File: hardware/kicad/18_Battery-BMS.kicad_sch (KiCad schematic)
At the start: 29 parts, among them U80 BQ7694202PFBR

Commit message: starting erc check
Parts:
- C110, C111, C112, C113, C114, C119, C121: footprint Capacitor_SMD:C_0603_1608Metric -> 5v rail sm-easyedapro:C0603
- C115: footprint Capacitor_SMD:C_0603_1608Metric -> 5v rail sm-easyedapro:C0402; LCSC Part Name (none) -> 100pF ±5% 50V; Manufacturer (none) -> FOJAN(富捷); Manufacturer Part (none) -> FCC0402N101J500AT; Supplier (none) -> LCSC; Supplier Part (none) -> C5137573
- C120: footprint Capacitor_SMD:C_0603_1608Metric -> 5v rail sm-easyedapro:C0603; Manufacturer SAMSUNG(三星) -> HRE(芯声); Manufacturer Part CL10B105KB8NQNC -> CGA0603X5R105K500JT; Supplier Part C5199872 -> C6119852
- D19, D20, D21, D22: footprint Diode_SMD:SOD-123 -> 5v rail sm-easyedapro:SOD-123_L2.8-W1.8-LS3.7-RD
- R172, R173, R174, R175, R185, R187, R191, R192, R193, R194, R195: footprint Resistor_SMD:R_0603_1608Metric -> 5v rail sm-easyedapro:R0603
- R190: footprint Resistor_SMD:R_1206_3216Metric -> 5v rail sm-easyedapro:R1206
- U80: footprint Package_QFP:TQFP-48_7x7mm_P0.5mm -> 5v rail sm-easyedapro:TQFP-48_L7.0-W7.0-P0.50-LS9.0-TL
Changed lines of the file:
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@@
 			)
 		)
-		(property "Footprint" "Diode_SMD:SOD-123"
+		(property "Footprint" "5v rail sm-easyedapro:SOD-123_L2.8-W1.8-LS3.7-RD"
 			(at 218.44 31.75 0)
 			(effects
@@
 			)
 		)
-		(property "Footprint" "Resistor_SMD:R_0603_1608Metric"
+		(property "Footprint" "5v rail sm-easyedapro:R0603"
 			(at 157.48 160.02 0)
 			(effects
@@
 			)
 		)
-		(property "Footprint" "Diode_SMD:SOD-123"
+		(property "Footprint" "5v rail sm-easyedapro:SOD-123_L2.8-W1.8-LS3.7-RD"
 			(at 60.96 128.27 0)
 			(effects
@@
 			)
 		)
-		(property "Footprint" "Resistor_SMD:R_0603_1608Metric"
+		(property "Footprint" "5v rail sm-easyedapro:R0603"
 			(at 62.23 90.17 0)
 			(effects
@@
 			)
 		)
-		(property "Footprint" "Package_QFP:TQFP-48_7x7mm_P0.5mm"
+		(property "Footprint" "5v rail sm-easyedapro:TQFP-48_L7.0-W7.0-P0.50-LS9.0-TL"
 			(at 220.98 95.25 0)
 			(effects
@@
 			)
 		)
-		(property "Footprint" "Resistor_SMD:R_0603_1608Metric"
+		(property "Footprint" "5v rail sm-easyedapro:R0603"
 			(at 184.15 161.29 0)
 			(effects
@@
 			)
 		)
-		(property "Footprint" "Capacitor_SMD:C_0603_1608Metric"
+		(property "Footprint" "5v rail sm-easyedapro:C0603"
 			(at 302.26 54.61 0)
 			(effects
@@
 			)
 		)
-		(property "Footprint" "Capacitor_SMD:C_0603_1608Metric"
+		(property "Footprint" "5v rail sm-easyedapro:C0603"
 			(at 275.59 53.34 0)
 			(effects
@@
 			)
 		)
-		(property "Footprint" "Resistor_SMD:R_0603_1608Metric"
+		(property "Footprint" "5v rail sm-easyedapro:R0603"
 			(at 62.23 55.88 0)
 			(effects
@@
 			)
 		)
-		(property "Footprint" "Capacitor_SMD:C_0603_1608Metric"
+		(property "Footprint" "5v rail sm-easyedapro:C0402"
 			(at 171.45 147.32 0)
 			(effects
@@
 			)
 		)
-		(property "Datasheet" ""
+		(property "Datasheet" "https://item.szlcsc.com/datasheet/FCC0402N101J500AT/5747025.html"
 			(at 171.45 147.32 0)
 			(effects
@@
 			)
 		)
-		(property "Description" ""
+		(property "Description" "Capacitance:100pF Tolerance:±5% Tolerance:±5% Voltage Rating:50V Temperature Coefficient:C0G"
 			(at 171.45 147.32 0)
 			(effects
@@
 			)
 		)
-		(property "Manufacturer Part" ""
+		(property "Manufacturer Part" "FCC0402N101J500AT"
 			(at 171.45 147.32 0)
 			(effects
@@
 			)
 		)
-		(property "Manufacturer" ""
+		(property "Manufacturer" "FOJAN(富捷)"
 			(at 171.45 147.32 0)
 			(effects
@@
 			)
 		)
-		(property "Supplier Part" ""
+		(property "Supplier Part" "C5137573"
 			(at 171.45 147.32 0)
 			(effects
@@
 			)
 		)
-		(property "Supplier" ""
+		(property "Supplier" "LCSC"
 			(at 171.45 147.32 0)
 			(effects
@@
 			)
 		)
-		(property "LCSC Part Name" ""
+		(property "LCSC Part Name" "100pF ±5% 50V"
 			(at 171.45 147.32 0)
 			(effects
@@
 			)
 		)
-		(property "Footprint" "Capacitor_SMD:C_0603_1608Metric"
+		(property "Footprint" "5v rail sm-easyedapro:C0603"
 			(at 99.06 128.27 0)
 			(effects
@@
 			)
 		)
-		(property "Footprint" "Capacitor_SMD:C_0603_1608Metric"
+		(property "Footprint" "5v rail sm-easyedapro:C0603"
 			(at 78.74 81.28 0)
 			(effects
@@
 			)
 		)
-		(property "Footprint" "Resistor_SMD:R_0603_1608Metric"
+		(property "Footprint" "5v rail sm-easyedapro:R0603"
 			(at 288.29 80.01 0)
 			(effects
@@
 			)
 		)
-		(property "Footprint" "Resistor_SMD:R_0603_1608Metric"
+		(property "Footprint" "5v rail sm-easyedapro:R0603"
 			(at 62.23 102.87 0)
 			(effects
@@
 			)
 		)
-		(property "Footprint" "Diode_SMD:SOD-123"
+		(property "Footprint" "5v rail sm-easyedapro:SOD-123_L2.8-W1.8-LS3.7-RD"
 			(at 218.44 44.45 0)
 			(effects
@@
 			)
 		)
-		(property "Footprint" "Resistor_SMD:R_0603_1608Metric"
+		(property "Footprint" "5v rail sm-easyedapro:R0603"
 			(at 275.59 97.79 0)
 			(effects
@@
 			)
 		)
-		(property "Footprint" "Capacitor_SMD:C_0603_1608Metric"
+		(property "Footprint" "5v rail sm-easyedapro:C0603"
 			(at 289.56 54.61 0)
 			(effects
@@
 			)
 		)
-		(property "Datasheet" "https://item.szlcsc.com/datasheet/CL10B105KB8NQNC/5885909.html"
+		(property "Datasheet" "https://item.szlcsc.com/datasheet/CGA0603X5R105K500JT/7062558.html"
 			(at 289.56 54.61 0)
 			(effects
@@
 			)
 		)
-		(property "Description" "Capacitance:1uF Tolerance:±10% Tolerance:±10% Voltage Rating:50V Temperature Coefficient:X7R"
+		(property "Description" "Capacitance:1uF Tolerance:±10% Tolerance:±10% Voltage Rating:50V Temperature Coefficient:X5R"
 			(at 289.56 54.61 90)
 			(effects
@@
 			)
 		)
-		(property "Manufacturer Part" "CL10B105KB8NQNC"
+		(property "Manufacturer Part" "CGA0603X5R105K500JT"
 			(at 289.56 54.61 0)
 			(effects
@@
 			)
 		)
-		(property "Manufacturer" "SAMSUNG(三星)"
+		(property "Manufacturer" "HRE(芯声)"
 			(at 289.56 54.61 0)
 			(effects
@@
 			)
 		)
-		(property "Supplier Part" "C5199872"
+		(property "Supplier Part" "C6119852"
 			(at 289.56 54.61 0)
 			(effects
@@
 			)
 		)
-		(property "Footprint" "Capacitor_SMD:C_0603_1608Metric"
+		(property "Footprint" "5v rail sm-easyedapro:C0603"
 			(at 171.45 135.89 0)
 			(effects
@@
 			)
 		)
-		(property "Footprint" "Diode_SMD:SOD-123"
+		(property "Footprint" "5v rail sm-easyedapro:SOD-123_L2.8-W1.8-LS3.7-RD"
 			(at 78.74 128.27 0)
 			(effects
@@
 			)
 		)
-		(property "Footprint" "Resistor_SMD:R_0603_1608Metric"
+		(property "Footprint" "5v rail sm-easyedapro:R0603"
 			(at 288.29 90.17 0)
 			(effects
@@
 			)
 		)
-		(property "Datasheet" ""
+		(property "Datasheet" "~"
 			(at 203.2 44.45 0)
 			(effects
@@
 			)
 		)
-		(property "Description" ""
+		(property "Description" "Jumper, 2-pole, open"
 			(at 203.2 44.45 0)
 			(effects
@@
 			)
 		)
-		(property "Footprint" "Resistor_SMD:R_0603_1608Metric"
+		(property "Footprint" "5v rail sm-easyedapro:R0603"
 			(at 275.59 106.68 0)
 			(effects
@@
 			)
 		)
-		(property "Footprint" "Resistor_SMD:R_0603_1608Metric"
+		(property "Footprint" "5v rail sm-easyedapro:R0603"
 			(at 62.23 73.66 0)
 			(effects
@@
 			)
 		)
-		(property "Footprint" "Resistor_SMD:R_0603_1608Metric"
+		(property "Footprint" "5v rail sm-easyedapro:R0603"
 			(at 318.77 111.76 0)
 			(effects
@@
 			)
 		)
-		(property "Footprint" "Resistor_SMD:R_1206_3216Metric"
+		(property "Footprint" "5v rail sm-easyedapro:R1206"
 			(at 245.11 44.45 0)
 			(effects
@@
 			)
 		)
-		(property "Footprint" "Capacitor_SMD:C_0603_1608Metric"
+		(property "Footprint" "5v rail sm-easyedapro:C0603"
 			(at 78.74 64.77 0)
 			(effects
@@
 			)
 		)
-		(property "Footprint" "Capacitor_SMD:C_0603_1608Metric"
+		(property "Footprint" "5v rail sm-easyedapro:C0603"
 			(at 111.76 96.52 0)
 			(effects

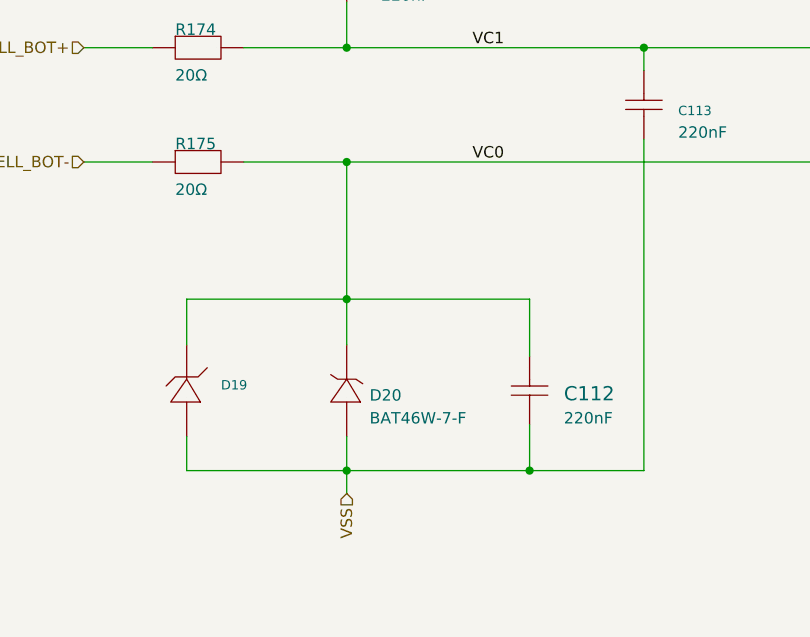
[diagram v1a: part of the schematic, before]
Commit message: usb c diodiding
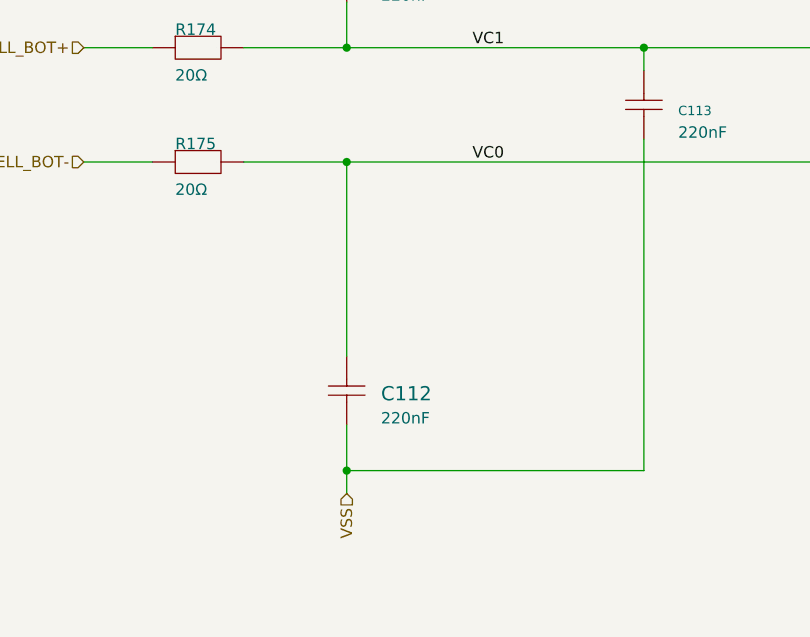
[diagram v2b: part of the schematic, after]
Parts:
- removed D19: MMSZ4685T1G, 5v rail sm-easyedapro:SOD-123_L2.8-W1.8-LS3.7-RD, symbol 5v rail sm-easyedapro:MMSZ4685T1G
- removed D20: BAT46W-7-F, 5v rail sm-easyedapro:SOD-123_L2.8-W1.8-LS3.7-RD, symbol 5v rail sm-easyedapro:BAT46W-7-F
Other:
- moved on the sheet: C112

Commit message: pre switching to native footprints for caps and resistors
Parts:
- removed C110, C111, C112, C113: 220nF, 5v rail sm-easyedapro:C0603, symbol 5v rail sm-easyedapro:CC0603KRX7R9BB224
- removed C121: 100pF, 5v rail sm-easyedapro:C0603, symbol 5v rail sm-easyedapro:CC0603JRNPO9BN101
- removed R172, R173, R174: 20Ω, 5v rail sm-easyedapro:R0603, symbol 5v rail sm-easyedapro:FRC0603F20R0TS
- removed R191: 82kΩ, 5v rail sm-easyedapro:R0603, symbol 5v rail sm-easyedapro:FRC0603F8202TS
- removed R192: 100kΩ, 5v rail sm-easyedapro:R0603, symbol 5v rail sm-easyedapro:FRC0603J104 TS
- removed R193, R194, R195: 10kΩ, 5v rail sm-easyedapro:R0603, symbol 5v rail sm-easyedapro:0603WAF1002T5E
- added C3501, C3502, C3503, C3505: 220nF, Capacitor_SMD:C_0402_1005Metric, symbol Device:C
- added C3504: 100pF, Capacitor_SMD:C_0402_1005Metric, symbol Device:C
- added R3501, R3502, R3503: 20Ω, Resistor_SMD:R_0603_1608Metric, symbol Device:R
- added R3504, R3505, R3508: 10k, Resistor_SMD:R_0402_1005Metric, symbol Device:R
- added R3506: 100k, Resistor_SMD:R_0402_1005Metric, symbol Device:R
- added R3507: 82k, Resistor_SMD:R_0402_1005Metric, symbol Device:R
- renumbered U79 to U?
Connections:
- net ALERT: now also R3508.1
- net ALERT_PULLUP: now also R3508.2
- net BAL-CELL-2: now also R3502.1
- net BAL-CELL-TOP: now also JP4.1 (A), R3501.1; no longer U?.2 (B)
- net BAL_CELL_BOT+: now also R3503.1
- net BQ-BAT: now also U?.2 (B); no longer JP4.1 (A)
- net PACK+: now also R3504.2, R3505.2
- net RST_SHUT: now also R3506.1
- net VC0: now also C3505.2
- net VC1: now also C3501.1, C3502.2, R3503.2
- net VC3: now also C3502.1, C3503.2, R3502.2
- net VC4: now also C3503.1, R3501.2
- net VSS: now also C3501.2, C3504.2, C3505.1, R3506.2, R3507.2
- net at D21.2: now also U?.1 (A); no longer JP4.2 (B)
- net at U80.34 (REG2), U80.35 (REG1): now also R3507.1
- net at U80.41 (LD): now also R3505.1
- net at U80.42 (PACK): now also R3504.1
- net at C119.2, C120.2, R190.1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: now also C3504.1
- net at D22.2: now also JP4.2 (B); no longer U?.1 (A)

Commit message: updating symbols to use kicad footprints where possible
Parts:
- C114, C119, C120: footprint 5v rail sm-easyedapro:C0603 -> Capacitor_SMD:C_0603_1608Metric
- C115: footprint 5v rail sm-easyedapro:C0402 -> Capacitor_SMD:C_0402_1005Metric
- R175, R185, R187: footprint 5v rail sm-easyedapro:R0603 -> Resistor_SMD:R_0603_1608Metric
- R190: footprint 5v rail sm-easyedapro:R1206 -> Resistor_SMD:R_1206_3216Metric
- gave numbers to parts that had none: 1
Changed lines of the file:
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@@
 			)
 		)
-		(property "Footprint" "5v rail sm-easyedapro:R0603"
+		(property "Footprint" "Resistor_SMD:R_0603_1608Metric"
 			(at 157.48 160.02 0)
 			(effects
@@
 			)
 		)
-		(property "Footprint" "5v rail sm-easyedapro:R0603"
+		(property "Footprint" "Resistor_SMD:R_0603_1608Metric"
 			(at 184.15 161.29 0)
 			(effects
@@
 			)
 		)
-		(property "Footprint" "5v rail sm-easyedapro:C0603"
+		(property "Footprint" "Capacitor_SMD:C_0603_1608Metric"
 			(at 275.59 53.34 0)
 			(effects
@@
 			)
 		)
-		(property "Footprint" "5v rail sm-easyedapro:C0402"
+		(property "Footprint" "Capacitor_SMD:C_0402_1005Metric"
 			(at 171.45 147.32 0)
 			(effects
@@
 			)
 		)
-		(property "Footprint" "5v rail sm-easyedapro:R0603"
+		(property "Footprint" "Resistor_SMD:R_0603_1608Metric"
 			(at 62.23 102.87 0)
 			(effects
@@
 			)
 		)
-		(property "Footprint" "5v rail sm-easyedapro:C0603"
+		(property "Footprint" "Capacitor_SMD:C_0603_1608Metric"
 			(at 289.56 54.61 0)
 			(effects
@@
 			)
 		)
-		(property "Footprint" "5v rail sm-easyedapro:C0603"
+		(property "Footprint" "Capacitor_SMD:C_0603_1608Metric"
 			(at 171.45 135.89 0)
 			(effects
@@
 		(on_board yes)
 		(dnp no)
-		(property "Reference" "U?"
+		(property "Reference" "U3501"
 			(at 200.66 30.48 0)
 			(effects
@@
 			(project "svea_powerboard_rev3"
 				(path "/3f85abf4-0b95-4c4a-b7e9-06f59ca1ea3d/5c2e021f-c2d4-49e2-8c36-9a64f1f12001/8d05c3b8-20a4-4a7f-9b20-01f8d5d5be11"
-					(reference "U?")
+					(reference "U3501")
 					(unit 1)
 				)
@@
 			)
 		)
-		(property "Footprint" "5v rail sm-easyedapro:R1206"
+		(property "Footprint" "Resistor_SMD:R_1206_3216Metric"
 			(at 245.11 44.45 0)
 			(effects

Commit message: switched some more
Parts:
- D21, D22: footprint 5v rail sm-easyedapro:SOD-123_L2.8-W1.8-LS3.7-RD -> Diode_SMD:SOD-123
- U80: footprint 5v rail sm-easyedapro:TQFP-48_L7.0-W7.0-P0.50-LS9.0-TL -> Package_QFP:TQFP-48_7x7mm_P0.5mm
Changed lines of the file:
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@@
 			)
 		)
-		(property "Footprint" "5v rail sm-easyedapro:SOD-123_L2.8-W1.8-LS3.7-RD"
+		(property "Footprint" "Diode_SMD:SOD-123"
 			(at 218.44 31.75 0)
 			(effects
@@
 			)
 		)
-		(property "Footprint" "5v rail sm-easyedapro:TQFP-48_L7.0-W7.0-P0.50-LS9.0-TL"
+		(property "Footprint" "Package_QFP:TQFP-48_7x7mm_P0.5mm"
 			(at 220.98 95.25 0)
 			(effects
@@
 			)
 		)
-		(property "Footprint" "5v rail sm-easyedapro:SOD-123_L2.8-W1.8-LS3.7-RD"
+		(property "Footprint" "Diode_SMD:SOD-123"
 			(at 218.44 44.45 0)
 			(effects

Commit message: updated more footprints
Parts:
- JP4: footprint Jumper:SolderJumper-2_P1.3mm_Bridged_RoundedPad1.0x1.5mm -> Jumper:SolderJumper-2_P1.3mm_Bridged_Pad1.0x1.5mm
- U3501: footprint Jumper:SolderJumper-2_P1.3mm_Open_Pad1.0x1.5mm -> Jumper:SolderJumper-2_P1.3mm_Open_TrianglePad1.0x1.5mm
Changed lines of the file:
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@@
 			)
 		)
-		(property "Footprint" "Jumper:SolderJumper-2_P1.3mm_Bridged_RoundedPad1.0x1.5mm"
+		(property "Footprint" "Jumper:SolderJumper-2_P1.3mm_Bridged_Pad1.0x1.5mm"
 			(at 203.2 44.45 0)
 			(effects
@@
 			)
 		)
-		(property "Footprint" "Jumper:SolderJumper-2_P1.3mm_Open_Pad1.0x1.5mm"
+		(property "Footprint" "Jumper:SolderJumper-2_P1.3mm_Open_TrianglePad1.0x1.5mm"
 			(at 203.2 31.75 0)
 			(effects

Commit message: starting erc check
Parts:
- D21, D22: footprint Diode_SMD:SOD-123 -> Diode_SMD:D_SOD-123
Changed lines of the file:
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@@
 			)
 		)
-		(property "Footprint" "Diode_SMD:SOD-123"
+		(property "Footprint" "Diode_SMD:D_SOD-123"
 			(at 218.44 31.75 0)
 			(effects
@@
 			)
 		)
-		(property "Footprint" "Diode_SMD:SOD-123"
+		(property "Footprint" "Diode_SMD:D_SOD-123"
 			(at 218.44 44.45 0)
 			(effects

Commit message: another update
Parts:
- added LED9: XL-1608UOC-06, LED_SMD:LED_0603_1608Metric, symbol JLCImport:XL-1608UOC-06
- added Q3: L2N7002SLLT1G, Package_TO_SOT_SMD:SOT-23, symbol 5v rail sm-easyedapro:L2N7002SLLT1G
- added R20: 220, Resistor_SMD:R_0603_1608Metric, symbol Device:R
- added R21: 100kΩ, Resistor_SMD:R_0402_1005Metric, symbol 5v rail sm-easyedapro:FRC0603J104 TS
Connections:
- net ALERT_PULLUP: now also R20.1
- new net: LED9.1 (K), R20.2
- new net BQ/ALERT: Q3.1 (G), R21.1
- new net BQ/ALERT/LED: LED9.2 (A), Q3.3 (D)
- new net GND: Q3.2 (S), R21.2
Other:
- note added: "4.5mA"
